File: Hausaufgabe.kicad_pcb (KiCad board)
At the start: 2 copper layers, 152 x 82.5 mm, 20 parts, among them Q1 Q_Dual_NPN_NPN_E1B1C2E2B2C1, Q2 Q_Dual_NPN_NPN_E1B1C2E2B2C1, SW1 SW_SPST

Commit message: comment about change
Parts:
- D1, D2, D3, D4, D5, D6: footprint LED_SMD:LED_1206_3216Metric_ReverseMount_Hole1.8x2.4mm -> Custom reverse mount LED:custom reverse mount LED
- moved D1 5.32 mm to (106.0, 65.8)
- moved D2 5.30 mm to (131.2, 65.7)
- moved D3 5.28 mm to (153.3, 115.0)
- moved D6 5.26 mm to (202.7, 108.2)
- moved D4 5.23 mm to (161.8, 113.8)
- moved D5 5.18 mm to (196.4, 109.2)

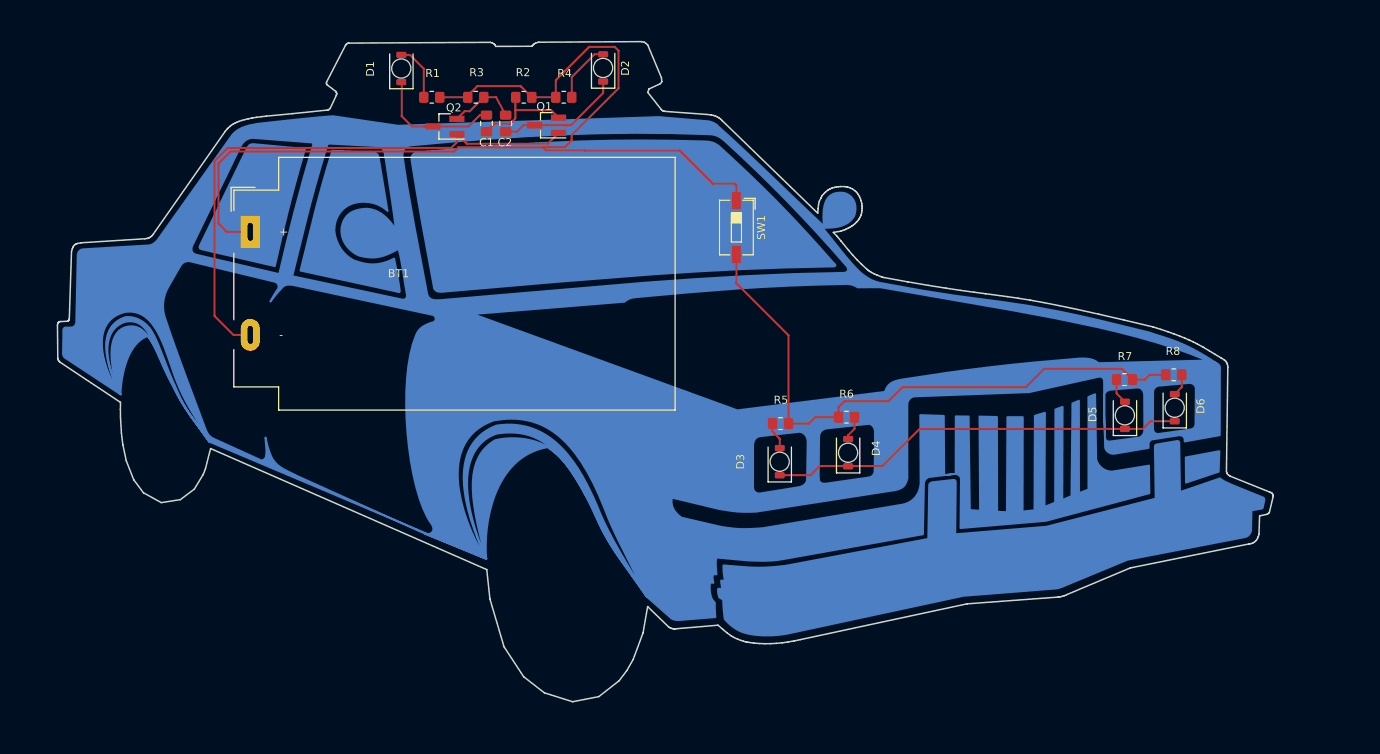
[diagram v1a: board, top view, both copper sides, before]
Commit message: fixed footprint and routing
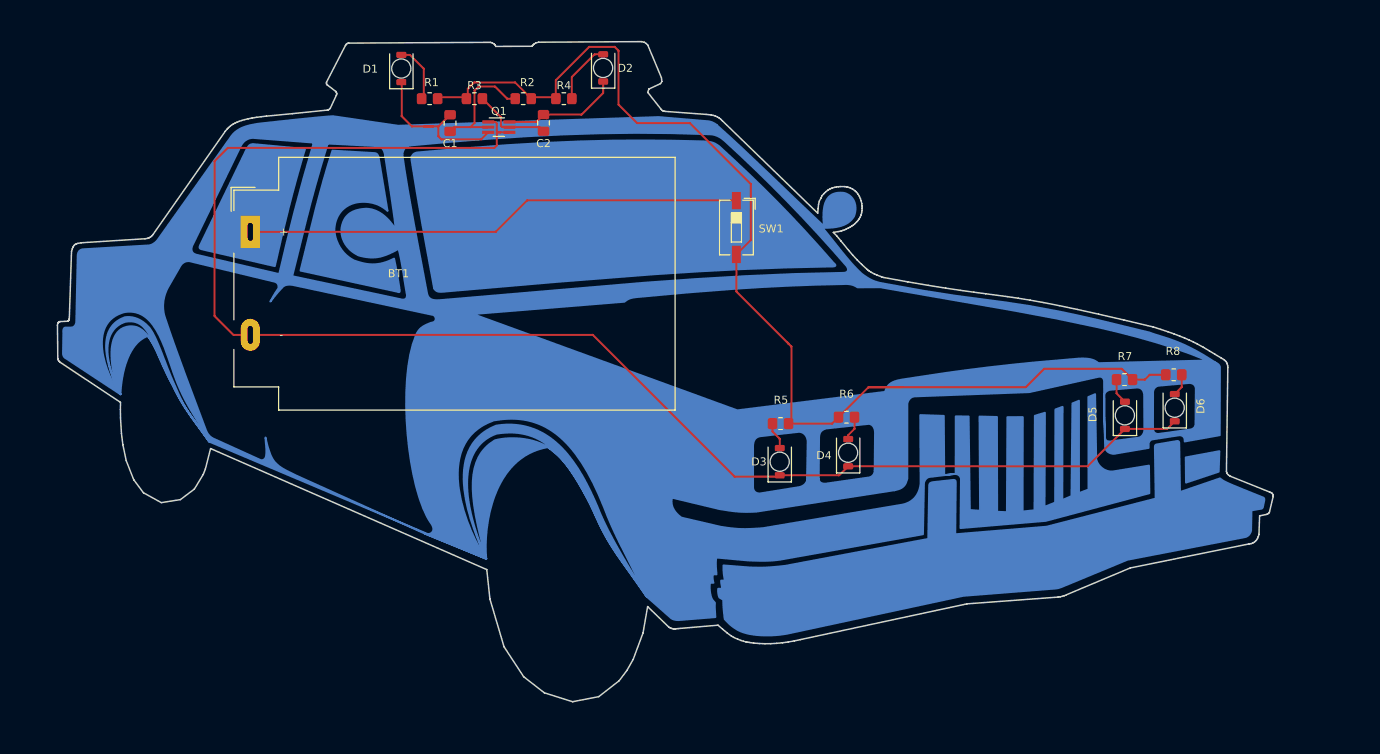
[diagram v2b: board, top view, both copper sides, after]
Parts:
- removed Q2: Q_Dual_NPN_NPN_E1B1C2E2B2C1, Package_TO_SOT_SMD:SOT-23_Handsoldering
- Q1: footprint Package_TO_SOT_SMD:SOT-23_Handsoldering -> Package_TO_SOT_SMD:SOT-363_SC-70-6_Handsoldering
- moved Q1 5.97 mm to (123.4, 73.2), turned to 0 degrees
- moved C2 4.73 mm to (129.0, 72.6), turned to -90 degrees
- moved C1 4.55 mm to (117.3, 72.6)
- moved R1 0.32 mm to (114.8, 69.6)
- moved R3 0.24 mm to (120.4, 69.6)
- moved R2 0.19 mm to (126.5, 69.6)
- moved R4 0.18 mm to (131.6, 69.6)
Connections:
- BT1 pad 2: Net-(BT1-Pad2) -> GND
- D3 pad 1: Net-(D3-Pad1) -> GND
- D4 pad 1: Net-(D3-Pad1) -> GND
- D5 pad 1: Net-(D3-Pad1) -> GND
- D6 pad 1: Net-(D3-Pad1) -> GND
- Q1 pad 1: Net-(BT1-Pad2) -> GND
- R1 pad 1: Net-(BT1-Pad1) -> +9V
- R2 pad 1: Net-(BT1-Pad1) -> +9V
- R3 pad 1: Net-(BT1-Pad1) -> +9V
- R4 pad 1: Net-(BT1-Pad1) -> +9V
- R5 pad 2: Net-(R1-Pad1) -> +9V
- R6 pad 2: Net-(R1-Pad1) -> +9V
- R7 pad 2: Net-(R1-Pad1) -> +9V
- R8 pad 2: Net-(R1-Pad1) -> +9V
- SW1 pad 2: Net-(R1-Pad1) -> +9V
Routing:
- net GND: track 0.00 -> 192.3 mm
- net +9V: track 0.00 -> 144.3 mm
- net Net-(R1-Pad1): track 75.4 -> 0.00 mm
- net Net-(BT1-Pad2): track 71.4 -> 0.00 mm
- net Net-(BT1-Pad1): track 126.6 -> 62.4 mm
- net Net-(D3-Pad1): track 52.2 -> 0.00 mm
- net Net-(C1-Pad1): track 17.1 -> 20.6 mm
- net Net-(C1-Pad2): track 12.8 -> 15.9 mm
- net Net-(C2-Pad1): track 16.2 -> 14.6 mm
- net Net-(C2-Pad2): track 8.70 -> 9.94 mm

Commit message: comment about change
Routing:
- net GND: track 192.3 -> 190.5 mm
- net +9V: track 144.3 -> 145.1 mm
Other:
- board text added: "Don't yeet the PCB!"

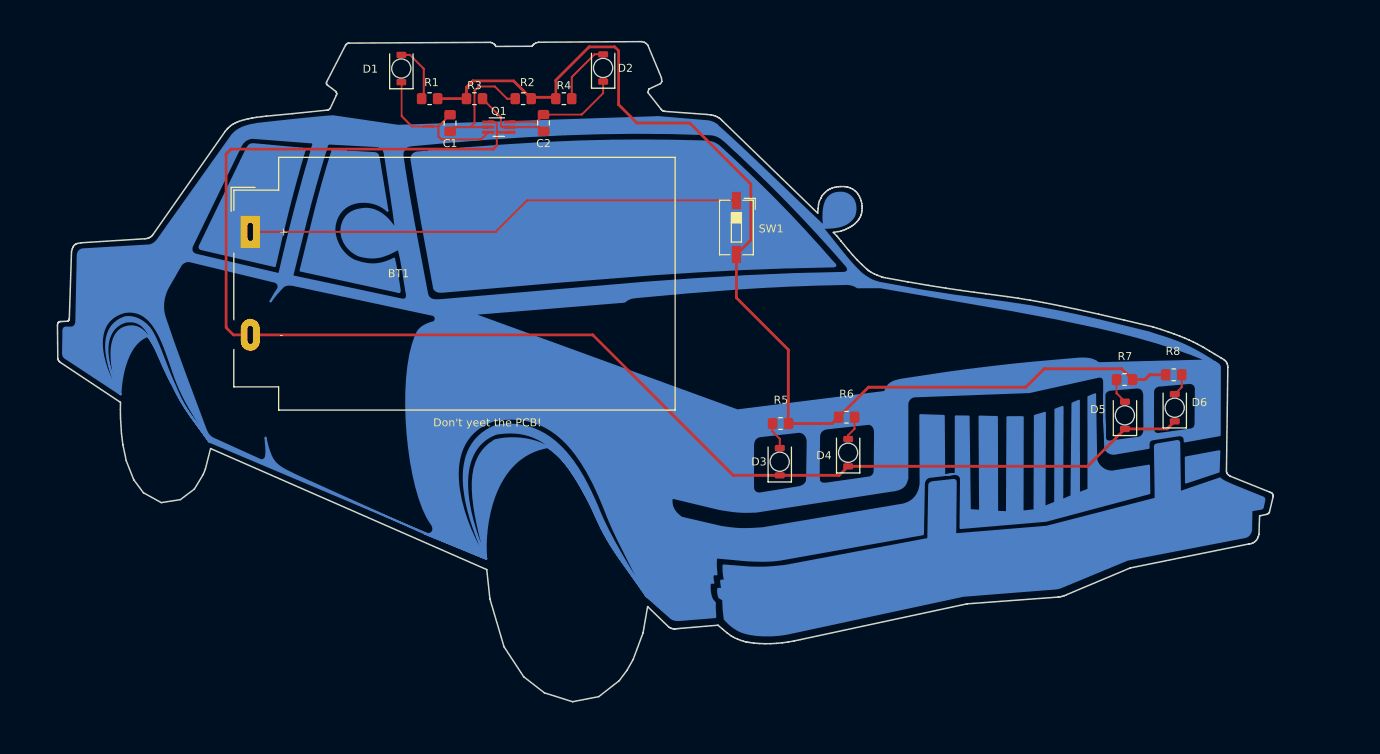
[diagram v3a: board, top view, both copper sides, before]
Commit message: changed LED and switch footprint, cleaned up frontside of board
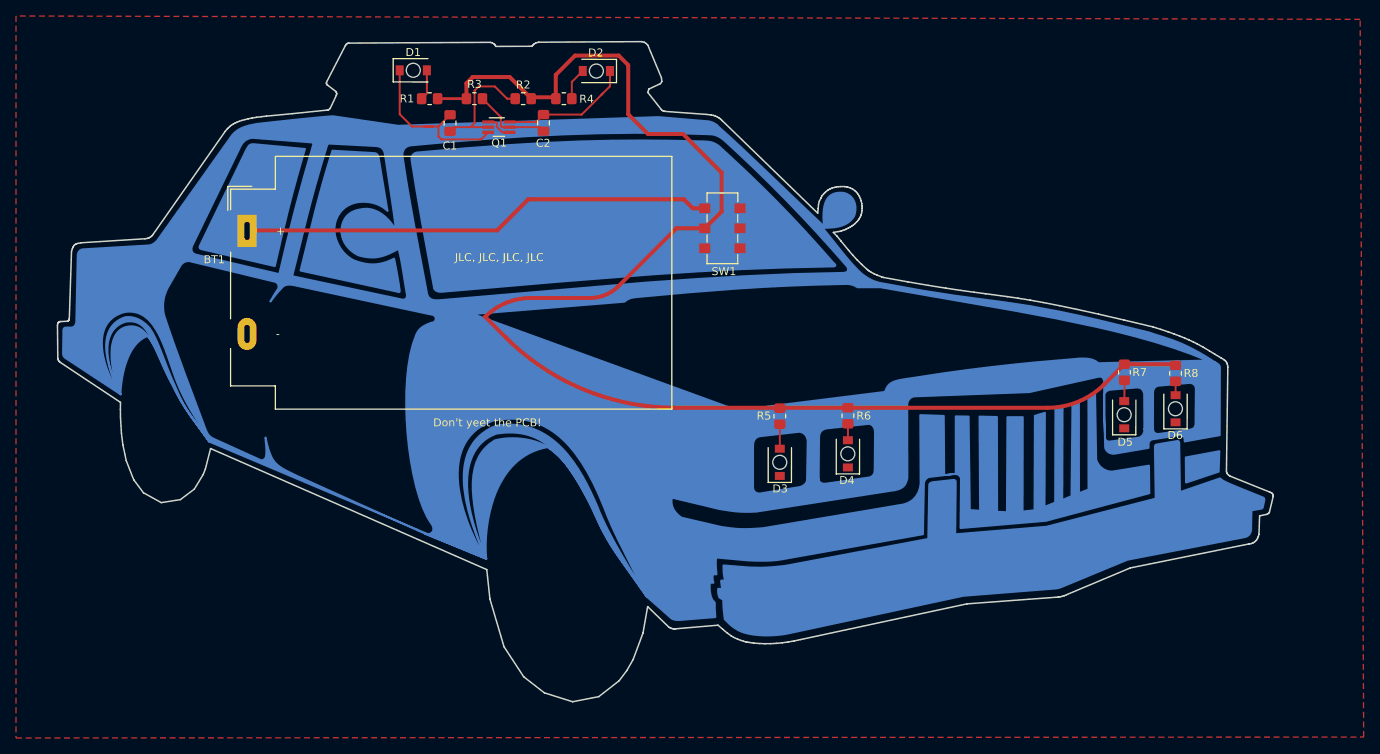
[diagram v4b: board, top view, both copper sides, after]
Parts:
- D1, D2, D3, D4, D5, D6: footprint Custom reverse mount LED:custom reverse mount LED -> Custom reverse mount LED:custom_reverse_mount_LED
- SW1: footprint Button_Switch_SMD:SW_DIP_SPSTx01_Slide_6.7x4.1mm_W6.73mm_P2.54mm_LowProfile_JPin -> Custom Slider Switch:CL-SB-22B
- moved D1 7.74 mm to (112.9, 62.4), turned to 0 degrees
- moved D2 5.91 mm to (135.5, 69.8), turned to 180 degrees
- moved SW1 1.80 mm to (151.3, 85.8), turned to 0 degrees
- moved D6 1.70 mm to (204.3, 108.2)
- moved D3 1.62 mm to (154.9, 114.9)
- moved D4 1.58 mm to (163.4, 113.8)
- moved D5 1.53 mm to (197.9, 108.9)
- moved R5 0.93 mm to (158.6, 109.3), turned to 90 degrees
- moved R7 0.92 mm to (201.6, 103.8), turned to 90 degrees
- moved BT1 0.43 mm to (110.5, 91.8)
- moved R8 0.29 mm to (208.0, 103.9), turned to 90 degrees
- moved R6 0.25 mm to (167.1, 109.2), turned to 90 degrees
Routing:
- net GND: track 190.5 -> 3.46 mm
- net +9V: track 145.1 -> 182.9 mm
- net Net-(D2-Pad2): track 7.63 -> 4.03 mm
- net Net-(D1-Pad2): track 7.09 -> 3.82 mm
- net Net-(BT1-Pad1): track 62.4 -> 59.3 mm
- net Net-(C2-Pad1): track 14.6 -> 16.6 mm
- net Net-(C1-Pad1): track 20.6 -> 22.1 mm
- net Net-(D6-Pad2): track 2.92 -> 1.73 mm
- net Net-(D4-Pad2): track 3.07 -> 2.06 mm
- net Net-(D5-Pad2): track 3.22 -> 2.62 mm
- added copper zone on F.Cu, net GND
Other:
- board text added: "JLC, JLC, JLC, JLC"
